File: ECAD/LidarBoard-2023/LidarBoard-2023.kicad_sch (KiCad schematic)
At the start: 17 parts, among them J1 Serial_Strategy, J2 Serial_Lidar, J3 Conn_01x03, J4 Oled, U1 Teensy3.2, U2 AMS1117-3.3

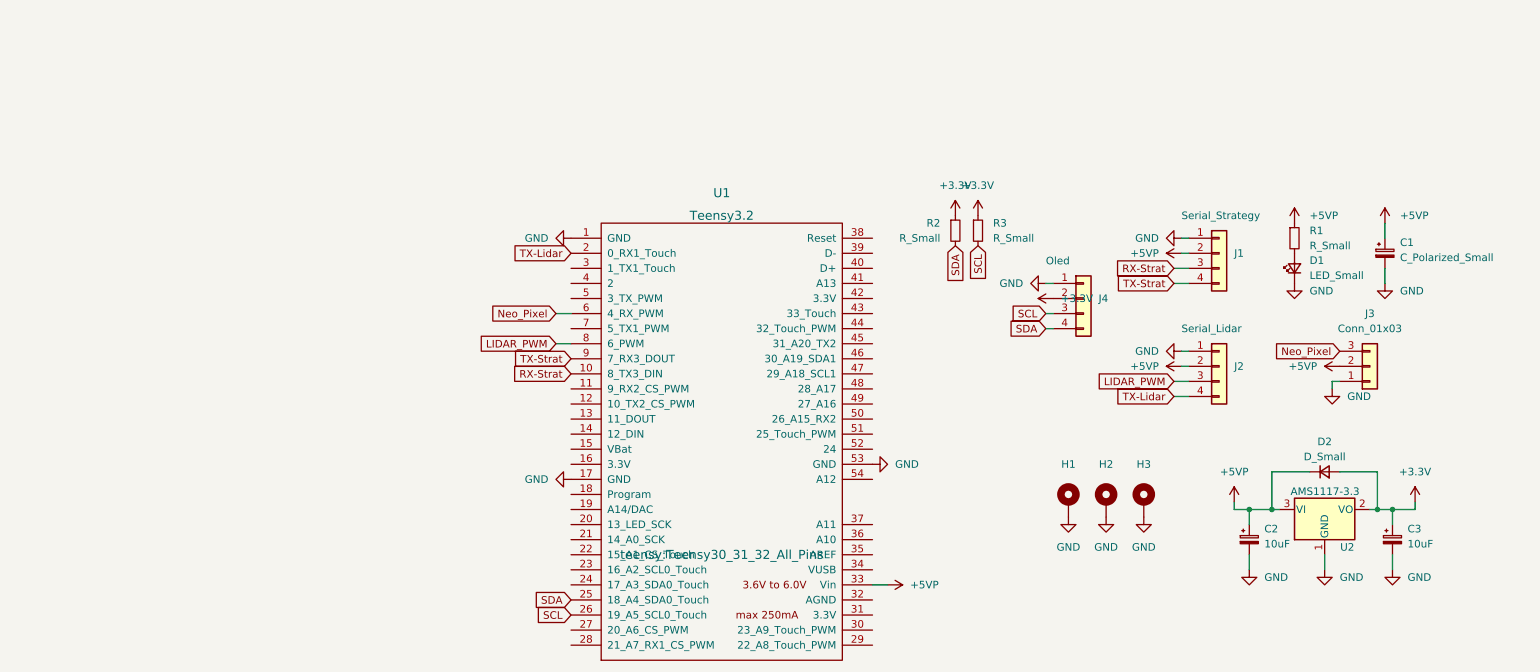
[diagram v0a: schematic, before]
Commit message: Capacitor & silkscreen
Change output capacitor type to tantalum 1206 - 22uF
Update Silkscreen before production
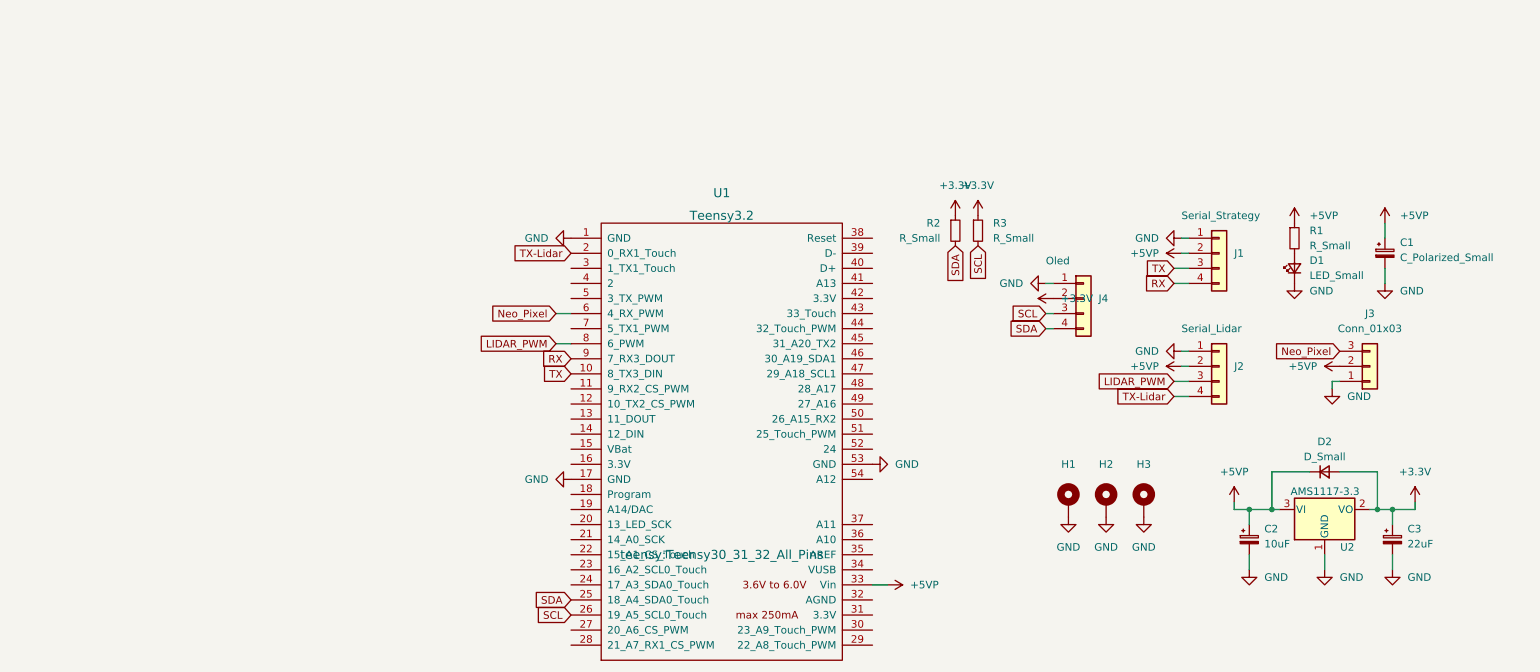
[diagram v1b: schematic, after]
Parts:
- C3: value 10uF -> 22uF; footprint Capacitor_SMD:CP_Elec_5x5.4 -> Capacitor_Tantalum_SMD:CP_EIA-3528-12_Kemet-T_Pad1.50x2.35mm_HandSolder
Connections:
- net RX-Strat renamed TX
- net TX-Strat renamed RX
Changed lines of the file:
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@@
     (stroke (width 0) (type default) (color 0 0 0 0))
   )
-  (global_label "RX-Strat" (shape input) (at 113.03 78.74 180) (fields_autoplaced)
-    (effects (font (size 1.27 1.27)) (justify right))
-    (property "Intersheet References" "${INTERSHEET_REFS}" (id 0) (at 101.9688 78.6606 0)
-      (effects (font (size 1.27 1.27)) (justify right) hide)
-    )
-  )
-  (global_label "TX-Strat" (shape input) (at 214.63 63.5 180) (fields_autoplaced)
-    (effects (font (size 1.27 1.27)) (justify right))
-    (property "Intersheet References" "${INTERSHEET_REFS}" (id 0) (at 203.8712 63.4206 0)
+  (global_label "TX" (shape input) (at 113.03 78.74 180) (fields_autoplaced)
+    (effects (font (size 1.27 1.27)) (justify right))
+    (property "Intersheet References" "${INTERSHEET_REFS}" (id 0) (at 108.4398 78.6606 0)
+      (effects (font (size 1.27 1.27)) (justify right) hide)
+    )
+  )
+  (global_label "RX" (shape input) (at 214.63 63.5 180) (fields_autoplaced)
+    (effects (font (size 1.27 1.27)) (justify right))
+    (property "Intersheet References" "${INTERSHEET_REFS}" (id 0) (at 209.7374 63.4206 0)
       (effects (font (size 1.27 1.27)) (justify right) hide)
     )
@@
     )
   )
-  (global_label "TX-Strat" (shape input) (at 113.03 76.2 180) (fields_autoplaced)
-    (effects (font (size 1.27 1.27)) (justify right))
-    (property "Intersheet References" "${INTERSHEET_REFS}" (id 0) (at 102.2712 76.1206 0)
+  (global_label "RX" (shape input) (at 113.03 76.2 180) (fields_autoplaced)
+    (effects (font (size 1.27 1.27)) (justify right))
+    (property "Intersheet References" "${INTERSHEET_REFS}" (id 0) (at 108.1374 76.1206 0)
       (effects (font (size 1.27 1.27)) (justify right) hide)
     )
@@
     )
   )
-  (global_label "RX-Strat" (shape input) (at 214.63 60.96 180) (fields_autoplaced)
-    (effects (font (size 1.27 1.27)) (justify right))
-    (property "Intersheet References" "${INTERSHEET_REFS}" (id 0) (at 203.5688 60.8806 0)
+  (global_label "TX" (shape input) (at 214.63 60.96 180) (fields_autoplaced)
+    (effects (font (size 1.27 1.27)) (justify right))
+    (property "Intersheet References" "${INTERSHEET_REFS}" (id 0) (at 210.0398 60.8806 0)
       (effects (font (size 1.27 1.27)) (justify right) hide)
     )
@@
       (effects (font (size 1.27 1.27)) (justify left))
     )
-    (property "Value" "10uF" (id 1) (at 254 107.4038 0)
-      (effects (font (size 1.27 1.27)) (justify left))
-    )
-    (property "Footprint" "Capacitor_SMD:CP_Elec_5x5.4" (id 2) (at 251.46 106.68 0)
+    (property "Value" "22uF" (id 1) (at 254 107.4038 0)
+      (effects (font (size 1.27 1.27)) (justify left))
+    )
+    (property "Footprint" "Capacitor_Tantalum_SMD:CP_EIA-3528-12_Kemet-T_Pad1.50x2.35mm_HandSolder" (id 2) (at 251.46 106.68 0)
       (effects (font (size 1.27 1.27)) hide)
     )
@@
     )
     (path "/c3d4710a-85df-4808-90d7-2bb91b5e40bc"
-      (reference "C3") (unit 1) (value "10uF") (footprint "Capacitor_SMD:CP_Elec_5x5.4")
+      (reference "C3") (unit 1) (value "22uF") (footprint "Capacitor_Tantalum_SMD:CP_EIA-3528-12_Kemet-T_Pad1.50x2.35mm_HandSolder")
     )
     (path "/17231e44-85ac-4aa3-a964-cf2197ceeee6"

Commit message: Change annotations
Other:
- company: (none) -> Les Karibous
- title: (none) -> Lidar Board 2023
- moved on the sheet: C1, C2, C3, D1, D2, H1, H2, H3, J1, J2, J3, J4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
